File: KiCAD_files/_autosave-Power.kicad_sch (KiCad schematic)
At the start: 63 parts, among them J101 2604-1102, J102 2604-1102, J103 2604-1102, J104 Conn_01x01, J105 Conn_01x01, J106 Conn_01x01, J107 Conn_01x01, J108 Conn_01x01, J109 Conn_01x01, J110 Conn_01x01, J111 Conn_01x01, J112 Conn_01x01, J113 Conn_01x01, J114 Conn_01x01, J115 Conn_01x01, J116 Conn_01x01, J117 2604-1102, J118 2604-1102, U101 AMC1311, U102 OPA316, U103 OPA316, U104 +-20A

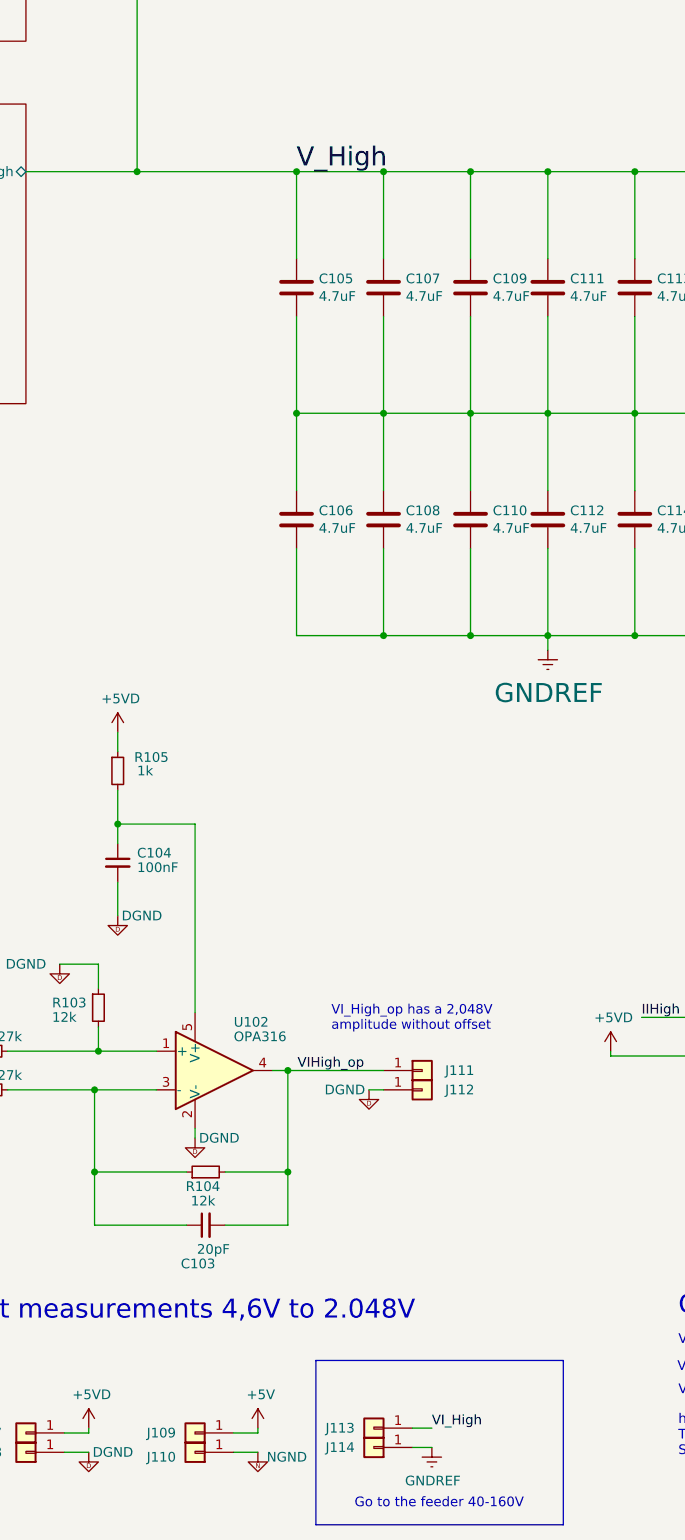
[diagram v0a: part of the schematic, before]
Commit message: [Power] Finished routing all the tracks, no more rastnet, ready for refining
Former-commit-id: c85419efed005dbd6b325ef0aef7156952f8cebe
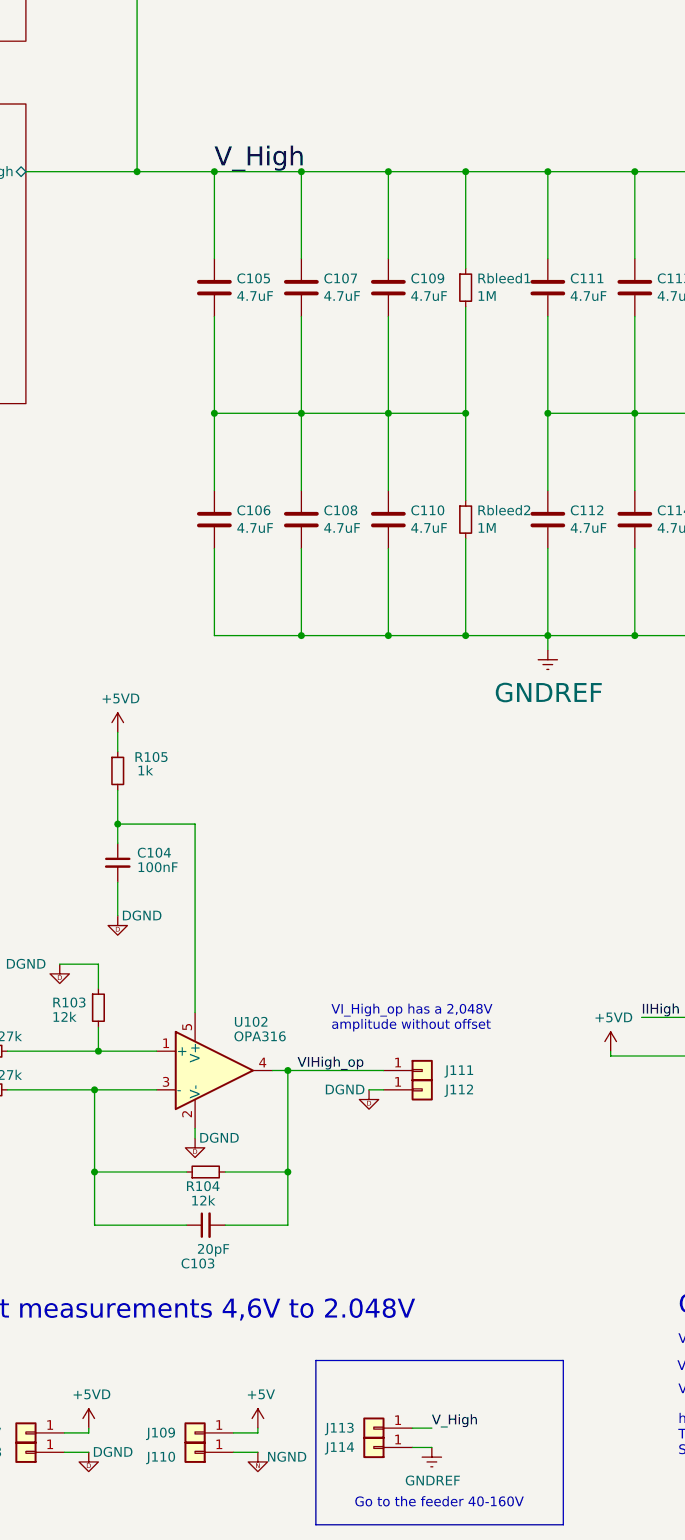
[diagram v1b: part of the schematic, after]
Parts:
- added Rbleed1, Rbleed2: 1M, Resistor_SMD:R_0805_2012Metric, symbol Device:R_Small
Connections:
- net GNDREF: now also Rbleed2.2
- net VI_High: no longer J113.1 (Pin_1)
- net V_High: now also J113.1 (Pin_1), Rbleed1.1
- net at C111.2, C112.1, C113.2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: no longer C105.2, C106.1, C107.2, C108.1, C109.2, C110.1
- new net: C105.2, C106.1, C107.2, C108.1, C109.2, C110.1, Rbleed1.2, Rbleed2.1
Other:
- moved on the sheet: C105, C106, C107, C108, C109, C110
